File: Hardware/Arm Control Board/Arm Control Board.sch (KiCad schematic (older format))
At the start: 14 parts

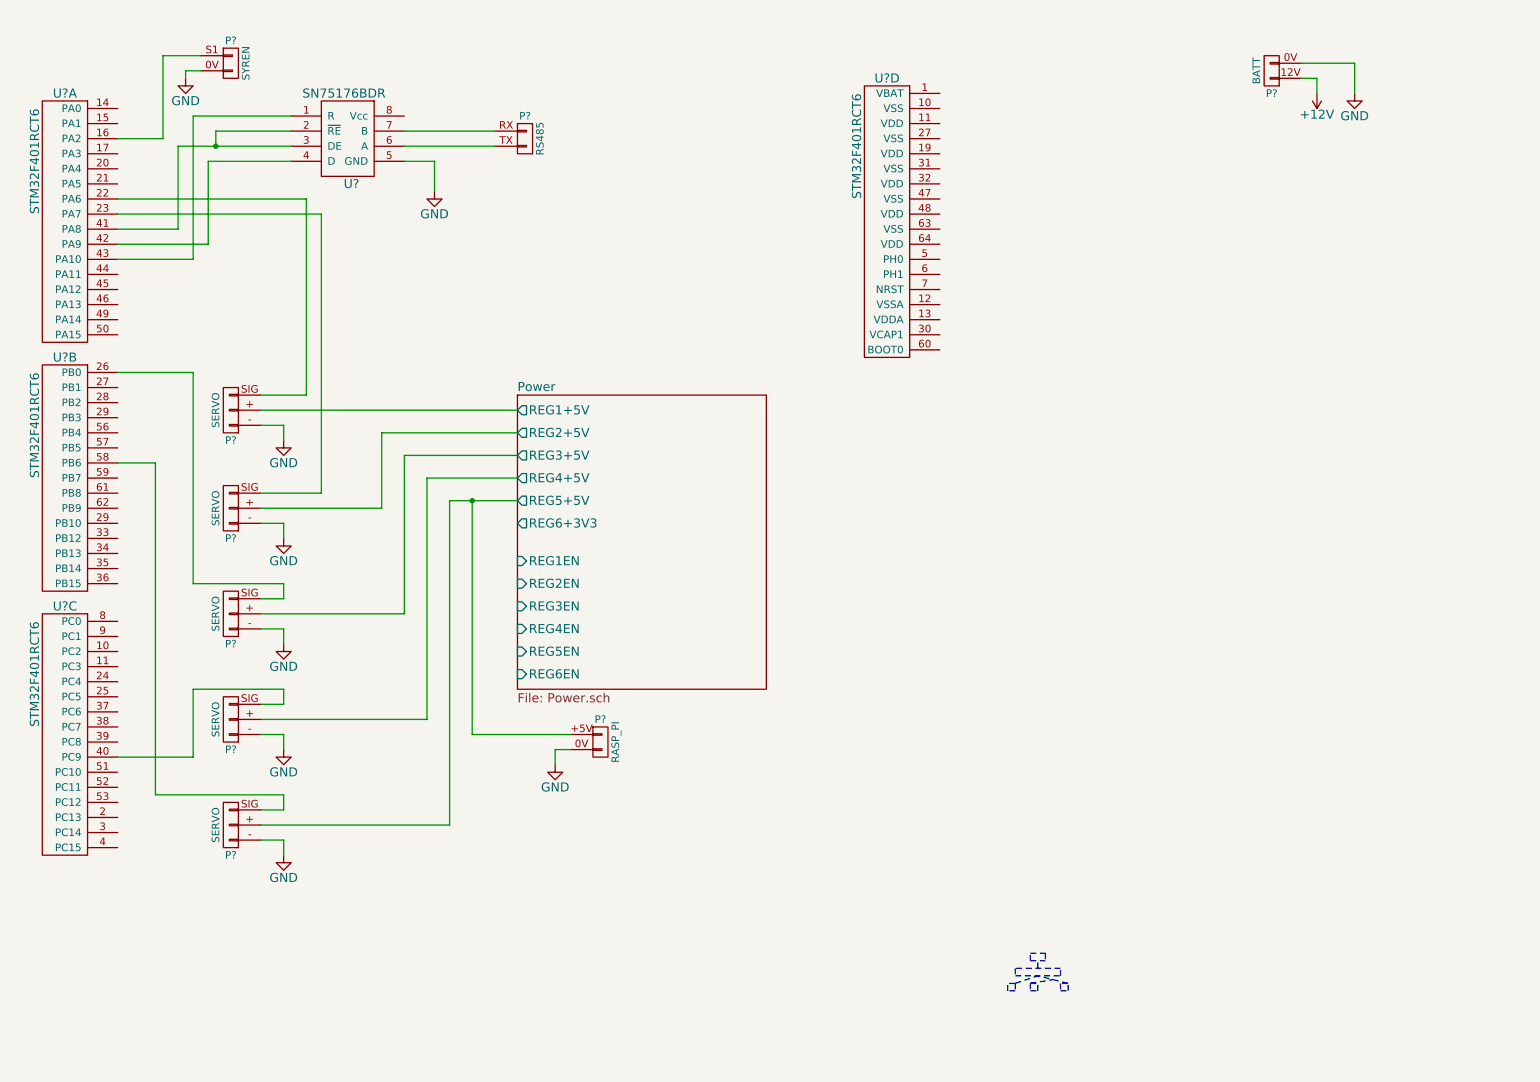
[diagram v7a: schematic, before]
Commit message: Added 74LVCH244APW buffer to servo lines
Able to push much more current than the micro can
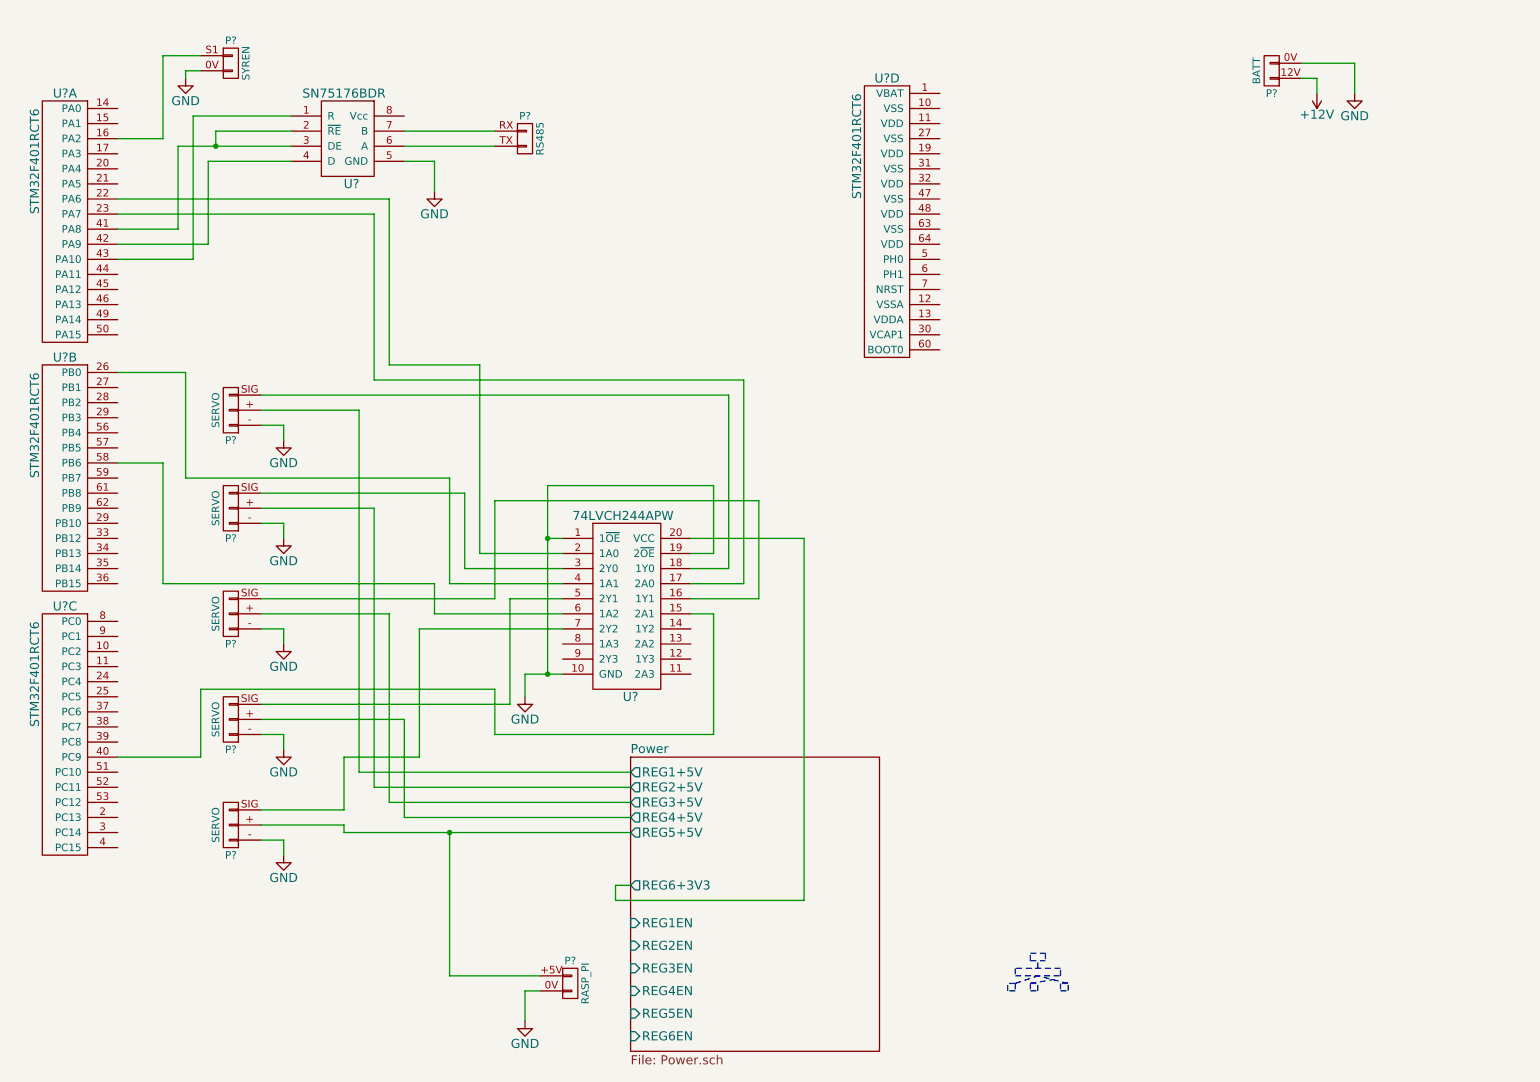
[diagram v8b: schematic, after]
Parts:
- added U?: 74LVCH244APW, symbol 74LVCH244APW
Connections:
- net GND: now also U?.1 (1~OE), U?.10 (GND), U?.19 (2~OE)
- net Power/REG6+3V3: now also U?.20 (VCC)
- net at P?.SIG: now also U?.18 (1Y0); no longer U?.22 (PA6)
- net at U?.23 (PA7): now also U?.17 (2A0); no longer P?.SIG
- net at P?.SIG: now also U?.16 (1Y1); no longer U?.26 (PB0)
- net at U?.40 (PC9): now also U?.15 (2A1); no longer P?.SIG
- net at U?.58 (PB6): now also U?.6 (1A2); no longer P?.SIG
- new net: U?.2 (1A0), U?.22 (PA6)
- new net: P?.SIG, U?.3 (2Y0)
- new net: U?.26 (PB0), U?.4 (1A1)
- new net: P?.SIG, U?.5 (2Y1)
- new net: P?.SIG, U?.7 (2Y2)
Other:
- moved on the sheet: P?
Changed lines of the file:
@@
 $EndComp
 $Sheet
-S 3850 2950 1650 1950
+S 4600 5350 1650 1950
 U 54C63434
 F0 "Power" 60
 F1 "Power.sch" 60
-F2 "REG1+5V" O L 3850 3050 60
-F3 "REG2+5V" O L 3850 3200 60
-F4 "REG3+5V" O L 3850 3350 60
-F5 "REG4+5V" O L 3850 3500 60
-F6 "REG5+5V" O L 3850 3650 60
-F7 "REG1EN" I L 3850 4050 60
-F8 "REG2EN" I L 3850 4200 60
-F9 "REG3EN" I L 3850 4350 60
-F10 "REG4EN" I L 3850 4500 60
-F11 "REG5EN" I L 3850 4650 60
-F12 "REG6+3V3" O L 3850 3800 60
-F13 "REG6EN" I L 3850 4800 60
+F2 "REG1+5V" O L 4600 5450 60
+F3 "REG2+5V" O L 4600 5550 60
+F4 "REG3+5V" O L 4600 5650 60
+F5 "REG4+5V" O L 4600 5750 60
+F6 "REG5+5V" O L 4600 5850 60
+F7 "REG1EN" I L 4600 6450 60
+F8 "REG2EN" I L 4600 6600 60
+F9 "REG3EN" I L 4600 6750 60
+F10 "REG4EN" I L 4600 6900 60
+F11 "REG5EN" I L 4600 7050 60
+F12 "REG6+3V3" O L 4600 6200 60
+F13 "REG6EN" I L 4600 7200 60
 $EndSheet
 $Comp
@@
 	9400 750  9400 950
 Wire Wire Line
-	3850 3050 2150 3050
-Wire Wire Line
-	3850 3200 2950 3200
-Wire Wire Line
-	2950 3200 2950 3700
-Wire Wire Line
-	2950 3700 2150 3700
-Wire Wire Line
-	3100 3350 3100 4400
-Wire Wire Line
-	3100 4400 2150 4400
-Wire Wire Line
-	3100 3350 3850 3350
-Wire Wire Line
-	3850 3500 3250 3500
-Wire Wire Line
-	3250 3500 3250 5100
-Wire Wire Line
-	3250 5100 2150 5100
-Wire Wire Line
-	3850 3650 3400 3650
-Wire Wire Line
-	3400 3650 3400 5800
-Wire Wire Line
-	3400 5800 2150 5800
+	2800 5450 4600 5450
+Wire Wire Line
+	4600 5550 2900 5550
+Wire Wire Line
+	2900 5550 2900 3700
+Wire Wire Line
+	2900 3700 2150 3700
+Wire Wire Line
+	3000 5650 3000 4400
+Wire Wire Line
+	3000 4400 2150 4400
+Wire Wire Line
+	3000 5650 4600 5650
+Wire Wire Line
+	4600 5750 3100 5750
+Wire Wire Line
+	3100 5750 3100 5100
+Wire Wire Line
+	3100 5100 2150 5100
+Wire Wire Line
+	2700 5850 4600 5850
+Wire Wire Line
+	3400 5850 3400 6800
 Wire Wire Line
 	2150 3150 2300 3150
@@
 	2300 5200 2150 5200
 Wire Wire Line
-	1200 1650 2450 1650
-Wire Wire Line
-	2450 1650 2450 2950
-Wire Wire Line
-	2450 2950 2150 2950
-Wire Wire Line
-	1200 1750 2550 1750
-Wire Wire Line
-	2550 1750 2550 3600
-Wire Wire Line
-	2550 3600 2150 3600
-Wire Wire Line
-	1200 2800 1700 2800
-Wire Wire Line
-	1700 2800 1700 4200
-Wire Wire Line
-	1700 4200 2300 4200
-Wire Wire Line
-	2300 4200 2300 4300
-Wire Wire Line
-	2300 4300 2150 4300
-Wire Wire Line
-	1200 5350 1700 5350
-Wire Wire Line
-	1700 5350 1700 4900
-Wire Wire Line
-	1700 4900 2300 4900
-Wire Wire Line
-	2300 4900 2300 5000
-Wire Wire Line
-	2300 5000 2150 5000
-Wire Wire Line
-	1200 3400 1450 3400
-Wire Wire Line
-	1450 3400 1450 5600
-Wire Wire Line
-	1450 5600 2300 5600
-Wire Wire Line
-	2300 5600 2300 5700
-Wire Wire Line
-	2300 5700 2150 5700
+	1200 1650 3000 1650
 Wire Notes Line
 	7150 6750 7150 6800
@@
 	1650 800  1650 850
 Wire Wire Line
-	3550 3650 3550 5200
-Wire Wire Line
-	3550 5200 4200 5200
-Connection ~ 3550 3650
+	3400 6800 4000 6800
+Connection ~ 3400 5850
 $Comp
 L RASP_PI P?
 U 1 1 54CA1701
-P 4400 5250
-F 0 "P?" H 4400 5400 50  0000 C CNN
-F 1 "RASP_PI" V 4500 5250 50  0000 C CNN
-F 2 "" H 4400 5250 60  0000 C CNN
-F 3 "" H 4400 5250 60  0000 C CNN
-	1    4400 5250
+P 4200 6850
+F 0 "P?" H 4200 7000 50  0000 C CNN
+F 1 "RASP_PI" V 4300 6850 50  0000 C CNN
+F 2 "" H 4200 6850 60  0000 C CNN
+F 3 "" H 4200 6850 60  0000 C CNN
+	1    4200 6850
 	1    0    0    -1
 $EndComp
@@
 L GND #PWR?
 U 1 1 54CA189F
-P 4100 5400
-F 0 "#PWR?" H 4100 5150 60  0001 C CNN
-F 1 "GND" H 4100 5250 60  0000 C CNN
-F 2 "" H 4100 5400 60  0000 C CNN
-F 3 "" H 4100 5400 60  0000 C CNN
-	1    4100 5400
-	1    0    0    -1
-$EndComp
-Wire Wire Line
-	4200 5300 4100 5300
-Wire Wire Line
-	4100 5300 4100 5400
+P 3900 7100
+F 0 "#PWR?" H 3900 6850 60  0001 C CNN
+F 1 "GND" H 3900 6950 60  0000 C CNN
+F 2 "" H 3900 7100 60  0000 C CNN
+F 3 "" H 3900 7100 60  0000 C CNN
+	1    3900 7100
+	1    0    0    -1
+$EndComp
 $Comp
 L STM32F401RCT6 U?
@@
 	1    0    0    -1
 $EndComp
+$Comp
+L 74LVCH244APW U?
+U 1 1 54C8472A
+P 5000 3900
+F 0 "U?" H 4600 2850 60  0000 C CNN
+F 1 "74LVCH244APW" H 4550 4050 60  0000 C CNN
+F 2 "" H 5000 3900 60  0000 C CNN
+F 3 "" H 5000 3900 60  0000 C CNN
+	1    5000 3900
+	1    0    0    -1
+$EndComp
+Wire Wire Line
+	3000 1650 3000 2750
+Wire Wire Line
+	5750 3900 5750 6300
+Wire Wire Line
+	5750 3900 5000 3900
+Wire Wire Line
+	4150 4800 3900 4800
+Wire Wire Line
+	3900 4800 3900 4950
+$Comp
+L GND #PWR?
+U 1 1 54C88705
+P 3900 4950
+F 0 "#PWR?" H 3900 4700 60  0001 C CNN
+F 1 "GND" H 3900 4800 60  0000 C CNN
+F 2 "" H 3900 4950 60  0000 C CNN
+F 3 "" H 3900 4950 60  0000 C CNN
+	1    3900 4950
+	1    0    0    -1
+$EndComp
+Wire Wire Line
+	4000 6900 3900 6900
+Wire Wire Line
+	3900 6900 3900 7100
+Wire Wire Line
+	2800 5450 2800 3050
+Wire Wire Line
+	2150 5800 2700 5800
+Wire Wire Line
+	2700 5800 2700 5850
+Wire Wire Line
+	4600 6200 4500 6200
+Wire Wire Line
+	4500 6200 4500 6300
+Wire Wire Line
+	4500 6300 5750 6300
+Wire Wire Line
+	2800 3050 2150 3050
+Wire Wire Line
+	3000 2750 3600 2750
+Wire Wire Line
+	3600 2750 3600 4000
+Wire Wire Line
+	3600 4000 4150 4000
+Wire Wire Line
+	5000 4100 5250 4100
+Wire Wire Line
+	5250 4100 5250 2950
+Wire Wire Line
+	5250 2950 2150 2950
+Wire Wire Line
+	1200 1750 2900 1750
+Wire Wire Line
+	2900 1750 2900 2850
+Wire Wire Line
+	2900 2850 5350 2850
+Wire Wire Line
+	5350 2850 5350 4200
+Wire Wire Line
+	5350 4200 5000 4200
+Wire Wire Line
+	4150 4100 3500 4100
+Wire Wire Line
+	3500 4100 3500 3600
+Wire Wire Line
+	3500 3600 2150 3600
+Wire Wire Line
+	1200 2800 1650 2800
+Wire Wire Line
+	1650 2800 1650 3500
+Wire Wire Line
+	1650 3500 3400 3500
+Wire Wire Line
+	3400 3500 3400 4200
+Wire Wire Line
+	3400 4200 4150 4200
+Wire Wire Line
+	5000 4300 5450 4300
+Wire Wire Line
+	5450 4300 5450 3650
+Wire Wire Line
+	5450 3650 3700 3650
+Wire Wire Line
+	3700 3650 3700 4300
+Wire Wire Line
+	3700 4300 2150 4300
+Wire Wire Line
+	1200 5350 1750 5350
+Wire Wire Line
+	1750 5350 1750 4900
+Wire Wire Line
+	1750 4900 3700 4900
+Wire Wire Line
+	3700 4900 3700 5200
+Wire Wire Line
+	3700 5200 5150 5200
+Wire Wire Line
+	5150 5200 5150 4400
+Wire Wire Line
+	5150 4400 5000 4400
+Wire Wire Line
+	4150 4300 3800 4300
+Wire Wire Line
+	3800 4300 3800 5000
+Wire Wire Line
+	3800 5000 2150 5000
+Wire Wire Line
+	1200 3400 1500 3400
+Wire Wire Line
+	1500 3400 1500 4200
+Wire Wire Line
+	1500 4200 3300 4200
+Wire Wire Line
+	3300 4200 3300 4400
+Wire Wire Line
+	3300 4400 4150 4400
+Wire Wire Line
+	4150 4500 3200 4500
+Wire Wire Line
+	3200 4500 3200 5350
+Wire Wire Line
+	3200 5350 2700 5350
+Wire Wire Line
+	2700 5350 2700 5700
+Wire Wire Line
+	2700 5700 2150 5700
+Wire Wire Line
+	4150 3900 4050 3900
+Wire Wire Line
+	4050 3550 4050 4800
+Connection ~ 4050 4800
+Wire Wire Line
+	5000 4000 5150 4000
+Wire Wire Line
+	5150 4000 5150 3550
+Wire Wire Line
+	5150 3550 4050 3550
+Connection ~ 4050 3900
 $EndSCHEMATC
